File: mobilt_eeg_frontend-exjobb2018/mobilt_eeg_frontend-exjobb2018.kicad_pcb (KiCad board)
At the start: 2 copper layers, 65 x 56 mm, 5 parts, among them P1 Conn_02x20_Odd_Even

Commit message: plz no crash now.
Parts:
- added C1: 0.1uF, Capacitors_SMD:C_0805_HandSoldering, F.Cu at (243.0, 114.7)
- added X1: X1G0044810050_SG7050CAN_2.048_MHZ, prj_lib_fp:SG0705, F.Cu at (248.4, 115.6)
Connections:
- P1 pad 1: +3V3 -> Net-(P1-Pad1)
- P1 pad 17: +3V3 -> Net-(P1-Pad17)
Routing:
- net +3V3: track 0.00 -> 11.0 mm
- net GND: track 0.00 -> 8.86 mm
- removed copper zone on F.Cu, net GND
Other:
- board size 65 x 56 mm -> 95 x 56 mm
- rule trace_min: 0.25 -> 0.15
- rule via_min_drill: 0.5 -> 0.3
- rule via_min_size: 0.8 -> 0.4

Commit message: Goodnight.
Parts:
- added U1: ADS1299-4PAG, xQFP_64_to_2.54mm_adapter, F.Cu at (213.5, 138.5)
- moved C1 21.0 mm to (222.0, 115.7)
- moved X1 21.0 mm to (227.4, 116.6)
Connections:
- P1 pad 1: Net-(P1-Pad1) -> +3V3
- P1 pad 17: Net-(P1-Pad17) -> +3V3
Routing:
- net /GPIO8(SPI0_CE_N): track 0.00 -> 18.3 mm
- net /GPIO11(SPI0_SCK): track 0.00 -> 18.3 mm
- net /GPIO9(SPI0_MISO): track 0.00 -> 18.0 mm
- net Net-(U1-Pad37): track 0.00 -> 10.6 mm
- net /GPIO10(SPI0_MOSI): track 0.00 -> 10.3 mm
- net GND: track 8.86 -> 0.14 mm
- net +5V: track 0.00 -> 2.54 mm
- added copper zone on F.Cu, net +5V

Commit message: did another bloody tutorial...
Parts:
- added J1: Conn_02x04_Odd_Even, Pin_Headers:Pin_Header_Straight_2x04_Pitch2.54mm, F.Cu at (196.0, 112.0)
- added R1: 10k, Resistors_SMD:R_0805_HandSoldering, F.Cu at (226.7, 115.6)
- added R2: 10k, Resistors_SMD:R_0805_HandSoldering, F.Cu at (230.0, 115.6)
- U1: footprint xQFP_64_to_2.54mm_adapter -> prj_lib_fp:xQFP_64_to_2.54mm_adapter
- moved C1 7.11 mm to (214.9, 115.7)
- moved X1 7.11 mm to (220.3, 116.6)
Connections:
- net GND renamed GNDD
- C1 pad 1: +3V3 -> /DVDD
- U1 pad 10: Net-(U1-Pad10) -> /IN1_P
- U1 pad 15: Net-(U1-Pad15) -> /IN1_N
- U1 pad 16: Net-(U1-Pad16) -> /IN1_P
- U1 pad 35: Net-(U1-Pad35) -> /~PWDN
- U1 pad 36: Net-(U1-Pad36) -> /~RESET
- U1 pad 48: Net-(U1-Pad48) -> /DVDD
- U1 pad 50: Net-(U1-Pad48) -> /DVDD
- U1 pad 9: Net-(U1-Pad9) -> /IN1_N
- X1 pad 1: +3V3 -> /DVDD
- X1 pad 4: +3V3 -> /DVDD
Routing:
- net /DVDD: track 0.00 -> 32.8 mm
- net GNDD: track 0.14 -> 32.1 mm
- net /GPIO1: track 0.00 -> 26.8 mm
- net /GPIO3: track 0.00 -> 26.8 mm
- net /GPIO2: track 0.00 -> 24.0 mm
- net /GPIO4: track 0.00 -> 22.8 mm
- net +3V3: track 11.0 -> 0.00 mm
- net /~PWDN: track 0.00 -> 9.30 mm
- net /~RESET: track 0.00 -> 7.11 mm
- added copper zone on F.Cu, net GNDD

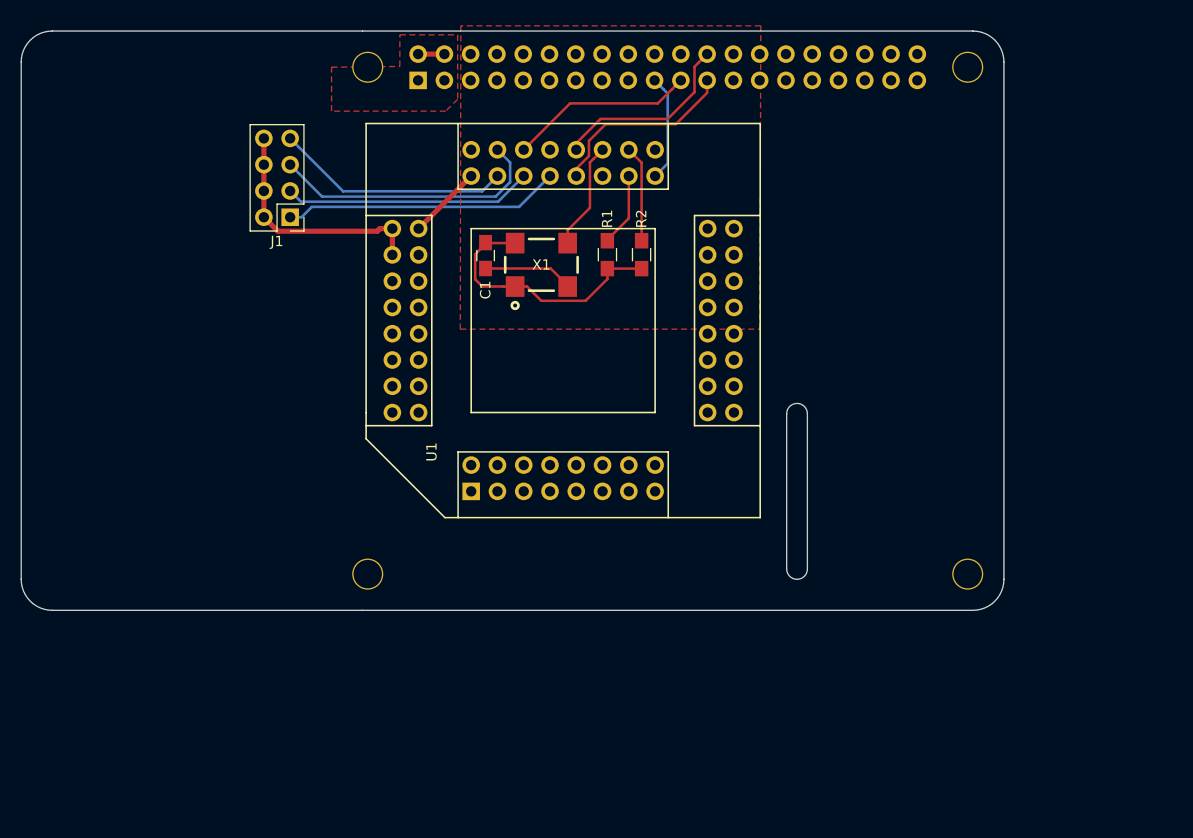
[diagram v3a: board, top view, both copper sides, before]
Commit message: added electrode intermediate pin-headers
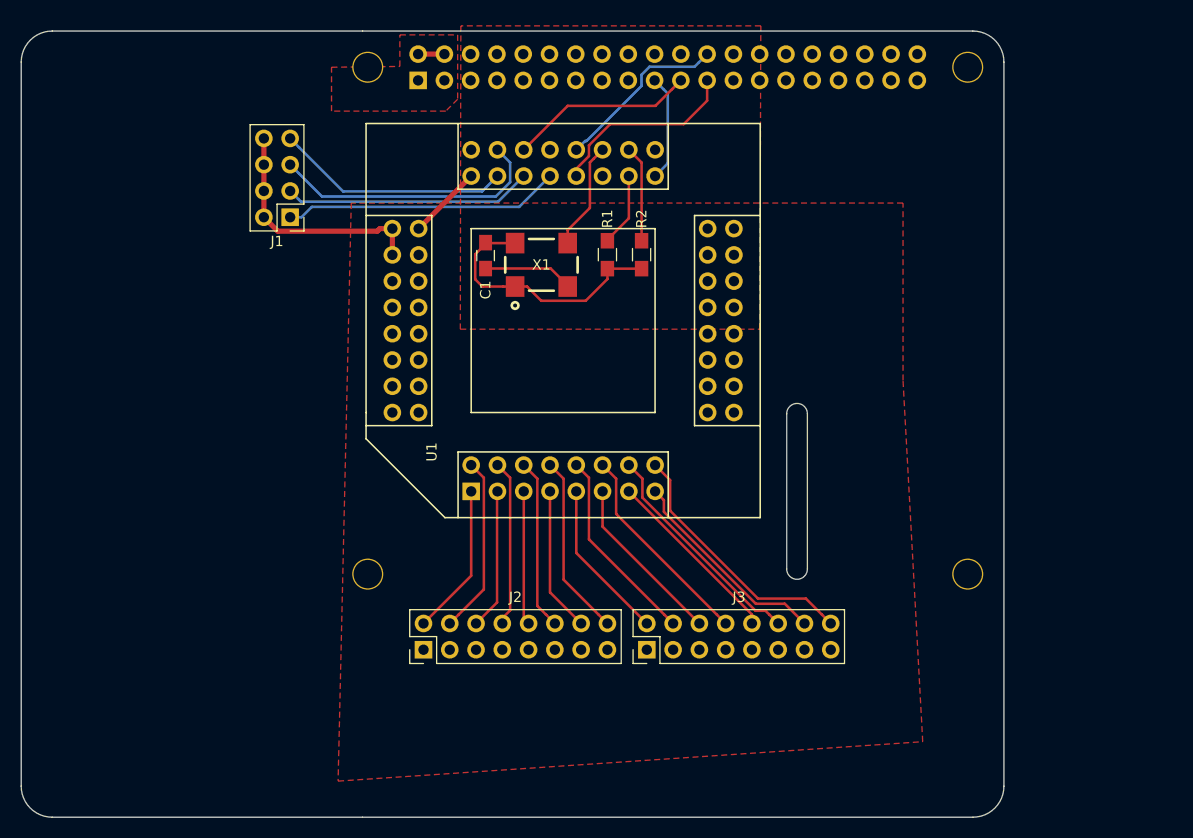
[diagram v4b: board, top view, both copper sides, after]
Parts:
- added J2: Conn_02x08_Odd_Even, Pin_Headers:Pin_Header_Straight_2x08_Pitch2.54mm, F.Cu at (208.9, 153.8)
- added J3: Conn_02x08_Odd_Even, Pin_Headers:Pin_Header_Straight_2x08_Pitch2.54mm, F.Cu at (230.5, 153.8)
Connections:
- U1 pad 10: /IN1_P -> Net-(J3-Pad4)
- U1 pad 15: /IN1_N -> Net-(J3-Pad14)
- U1 pad 16: /IN1_P -> Net-(J3-Pad16)
- U1 pad 9: /IN1_N -> Net-(J3-Pad2)
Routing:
- net Net-(J3-Pad16): track 0.00 -> 25.1 mm
- net Net-(J3-Pad12): track 0.00 -> 21.9 mm
- net Net-(J3-Pad14): track 0.00 -> 20.4 mm
- net Net-(J3-Pad8): track 0.00 -> 20.2 mm
- net Net-(J3-Pad4): track 0.00 -> 19.2 mm
- net Net-(J3-Pad10): track 0.00 -> 17.7 mm
- net Net-(J2-Pad16): track 0.00 -> 17.6 mm
- net Net-(J2-Pad4): track 0.00 -> 17.2 mm
- net Net-(J3-Pad6): track 0.00 -> 16.6 mm
- net Net-(J2-Pad12): track 0.00 -> 16.6 mm
- net Net-(J2-Pad8): track 0.00 -> 16.1 mm
- net Net-(J3-Pad2): track 0.00 -> 15.6 mm
- net Net-(J2-Pad2): track 0.00 -> 14.7 mm
- net Net-(J2-Pad14): track 0.00 -> 14.0 mm
- net Net-(J2-Pad6): track 0.00 -> 13.6 mm
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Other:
- board size 95 x 56 mm -> 95 x 76 mm

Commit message: done some stuff... it would be a shame if anything happened to it....
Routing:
- removed copper zone on F.Cu, net GNDD
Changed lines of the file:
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@@
   )
   (setup
-    (last_trace_width 0.15)
+    (last_trace_width 0.25)
     (user_trace_width 0.15)
     (user_trace_width 0.2)
@@
       )
     )
-  )
-  (zone (net 60) (net_name GNDD) (layer F.Cu) (hatch edge 0.508)
-    (connect_pads (clearance 0.254))
-    (min_thickness 0.254)
-    (fill yes (arc_segments 16) (thermal_gap 0.508) (thermal_bridge_width 0.508))
-    (polygon
-      (pts
-        (xy 212.5 93.5) (xy 212.446 122.822) (xy 241.402 122.822) (xy 241.5 93.5)
-      )
-    )
-  )
-  (zone (net 60) (net_name GNDD) (layer F.Cu) (hatch edge 0.508)
-    (connect_pads (clearance 0.254))
-    (min_thickness 0.254)
-    (fill yes (arc_segments 16) (thermal_gap 0.508) (thermal_bridge_width 0.508))
-    (polygon
-      (pts
-        (xy 255.245 127.775) (xy 255.245 110.63) (xy 201.905 110.63) (xy 200.635 166.51) (xy 257.15 162.7)
-      )
-    )

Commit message: beginning to understand the big picture... life, the universe, everything...
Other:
- board text added: "Mobilt EEG 2018.07 Rev.B"
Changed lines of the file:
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@@
   (general
     (thickness 1.6)
-    (drawings 49)
+    (drawings 54)
     (tracks 135)
     (zones 0)
@@
       (clearance 1.6))
   )
+  (gr_line (start 271 111) (end 271 105) (layer F.SilkS) (width 0.1))
+  (gr_line (start 281 111) (end 271 111) (layer F.SilkS) (width 0.1))
+  (gr_line (start 281 105) (end 281 111) (layer F.SilkS) (width 0.1))
+  (gr_line (start 271 105) (end 281 105) (layer F.SilkS) (width 0.1))
+  (gr_text "Mobilt EEG\n2018.07\nRev.B" (at 276 108) (layer F.SilkS)
+    (effects (font (size 1 1) (thickness 0.25)))
+  )
   (gr_arc (start 173 97) (end 173 94) (angle -90) (layer Edge.Cuts) (width 0.1))

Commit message: before importing netlist to PCBNEW
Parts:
- removed J2, J3: Conn_02x08_Odd_Even, Pin_Headers:Pin_Header_Straight_2x08_Pitch2.54mm
- moved C1 7.00 mm to (214.9, 122.7)
- moved R1 7.00 mm to (226.7, 122.6)
- moved R2 7.00 mm to (230.0, 122.6)
- moved U1 7.00 mm to (213.5, 145.5)
- moved X1 7.00 mm to (220.3, 123.6)
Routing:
- net /GPIO1: track 26.8 -> 0.00 mm
- net Net-(J3-Pad16): track 25.1 -> 0.00 mm
- net /GPIO2: track 24.0 -> 0.00 mm
- net /GPIO4: track 22.8 -> 0.00 mm
- net Net-(J3-Pad12): track 21.9 -> 0.00 mm
- net /GPIO3: track 26.8 -> 5.60 mm
- net Net-(J3-Pad14): track 20.4 -> 0.00 mm
- net Net-(J3-Pad8): track 20.2 -> 0.00 mm
- net Net-(J3-Pad4): track 19.2 -> 0.00 mm
- net /GPIO11(SPI0_SCK): track 18.7 -> 0.00 mm
- net /GPIO9(SPI0_MISO): track 18.0 -> 0.00 mm
- net Net-(J3-Pad10): track 17.7 -> 0.00 mm
- net Net-(J2-Pad16): track 17.6 -> 0.00 mm
- net Net-(J2-Pad4): track 17.2 -> 0.00 mm
- net /GPIO8(SPI0_CE_N): track 17.1 -> 0.00 mm
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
